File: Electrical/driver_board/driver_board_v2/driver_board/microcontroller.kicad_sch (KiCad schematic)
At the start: 28 parts, among them J1 USB_C_Receptacle_USB2.0_14P, U1 AMS1117-3.3, U1 STM32F446RETx, Y1 8Mhz

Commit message: Added full PSU architecture to driverboard
+24V In

+12V out
+5V out
+3.3V out
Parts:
- removed C13, C14: C, symbol Device:C
- removed D1: LED, symbol Device:LED
- removed R2: 1.5kΩ, symbol Device:R
- removed U1: AMS1117-3.3, Package_TO_SOT_SMD:SOT-223-3_TabPin2, symbol Regulator_Linear:AMS1117-3.3
- gave numbers to parts that had none: 3
- renumbered FB2 to FB1, R3 to R2, R1 to R3, R2 to R4

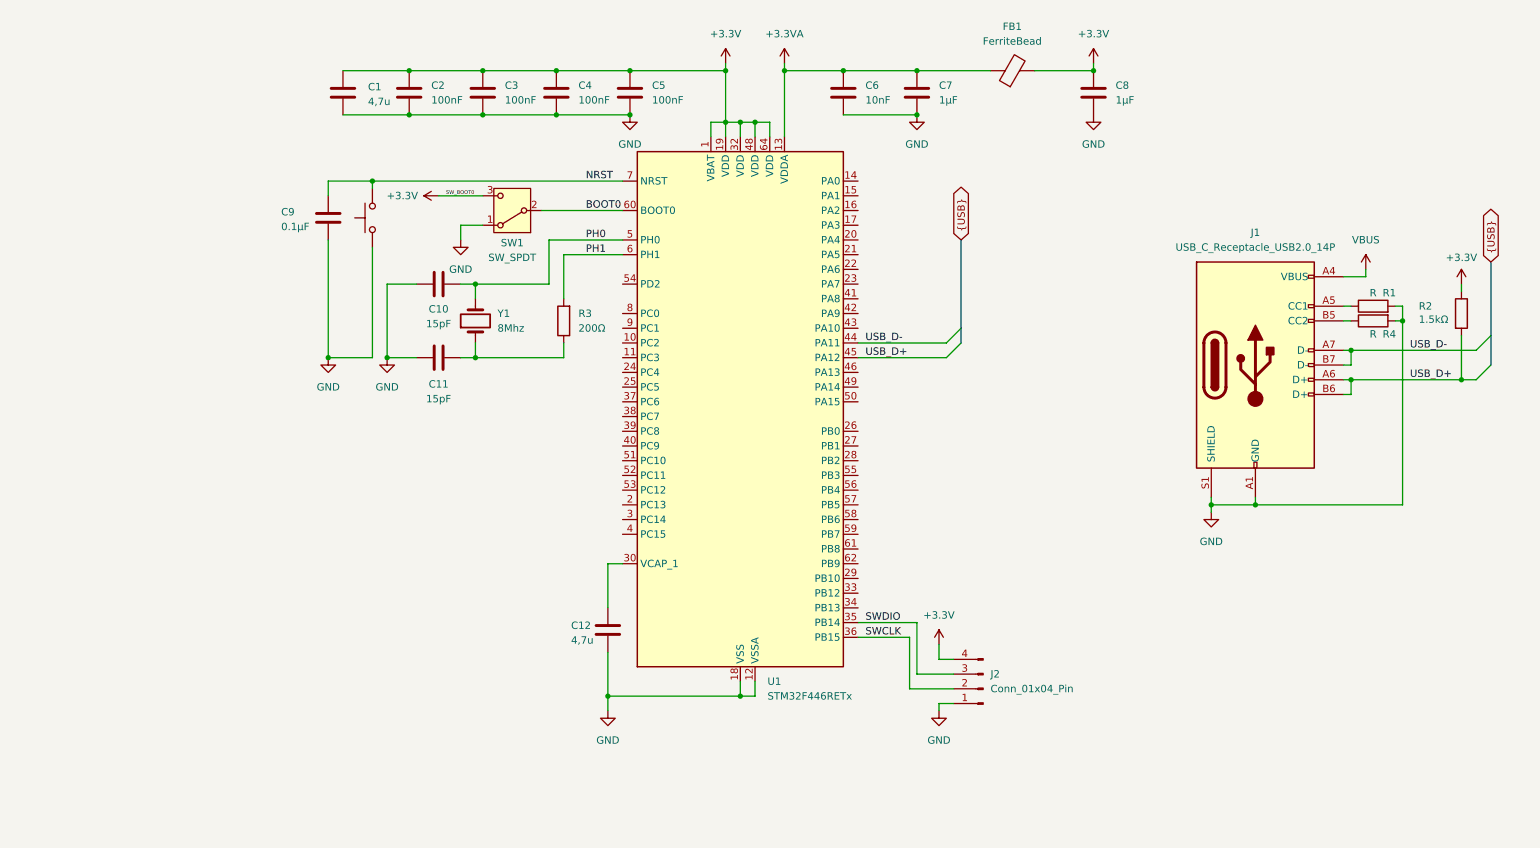
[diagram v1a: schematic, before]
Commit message: Cleaned up a bit and fixed mistake with NRST pin
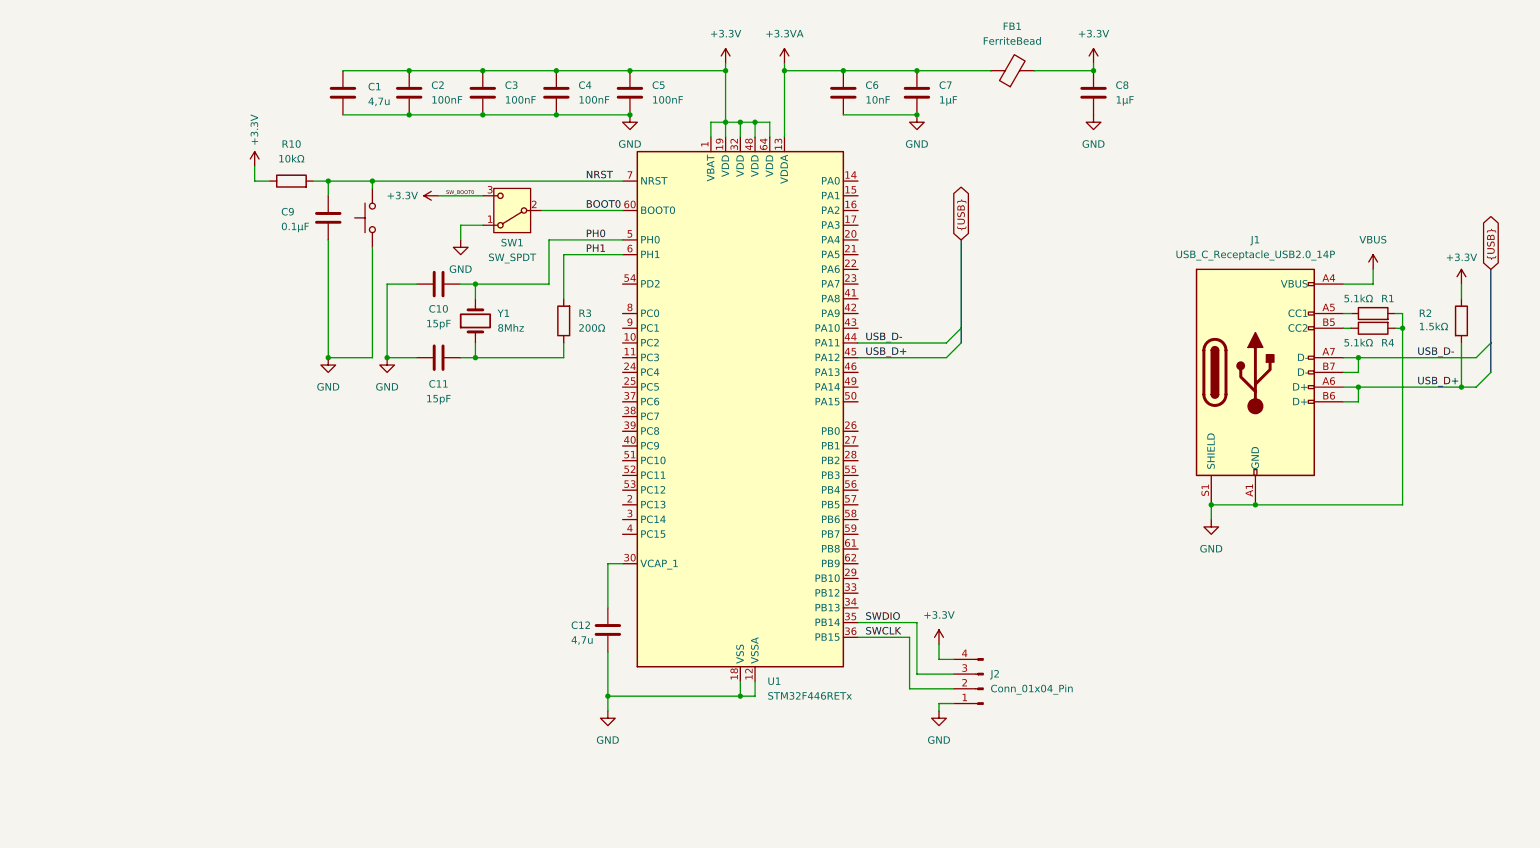
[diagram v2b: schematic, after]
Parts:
- added R10: 10kΩ, symbol Device:R
- R1, R4: value R -> 5.1kΩ
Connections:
- net +3.3V: now also R10.1
- net NRST: now also R10.2
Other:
- moved on the sheet: J1, R1, R2, R4

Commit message: Added footprint of motor driver and added power
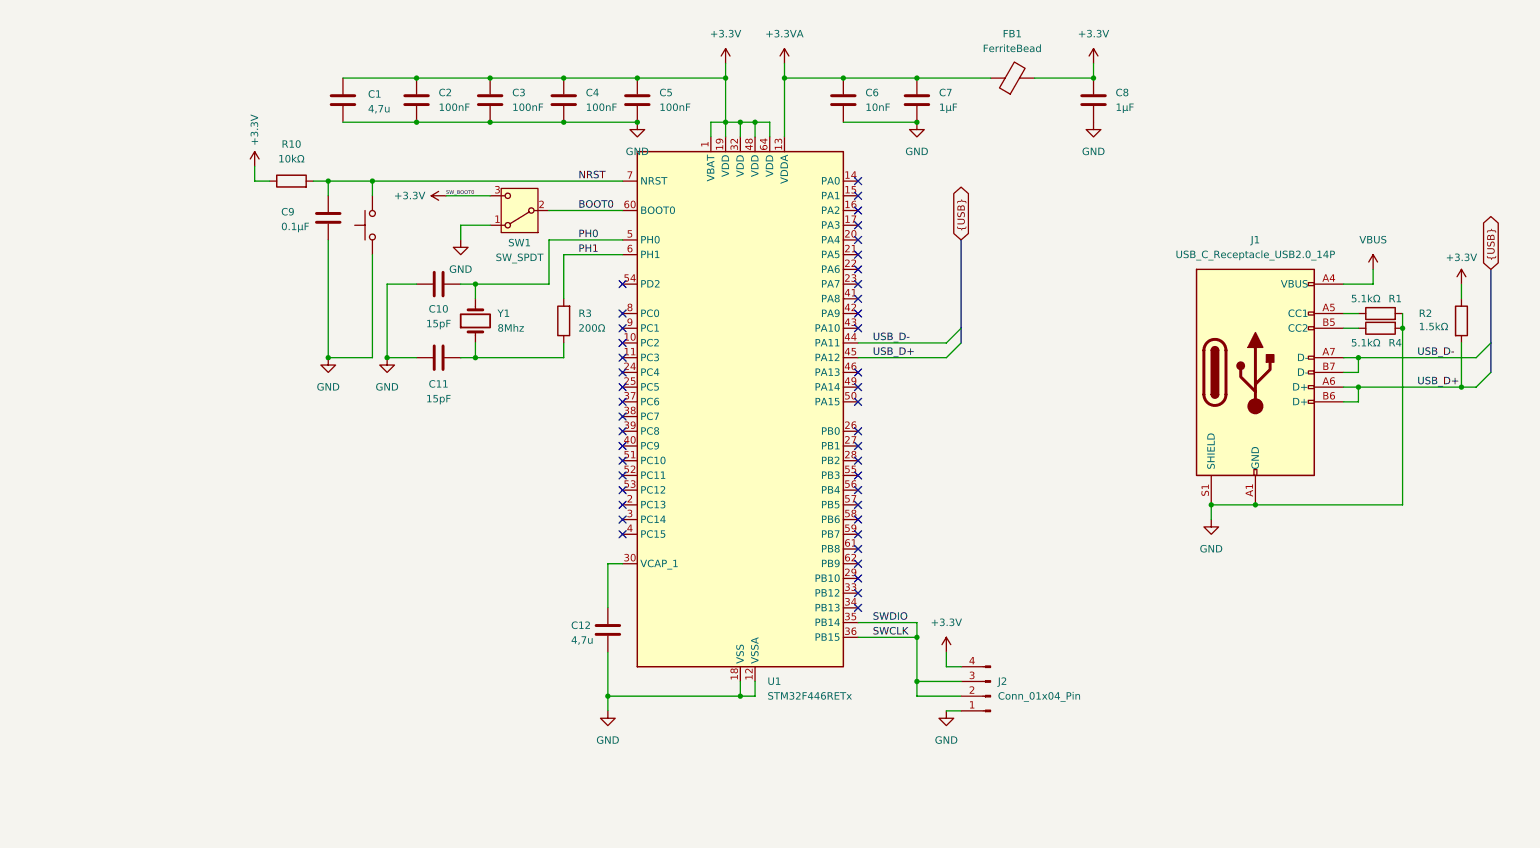
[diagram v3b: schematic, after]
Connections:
- net SWDIO is gone; now on net SWCLK: J2.3 (Pin_3), U1.35 (PB14)
- no-connect marks 0 -> 44
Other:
- moved on the sheet: C1, C2, C3, C4, C5, C6, C7, C8, FB1, J2, R1, R4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

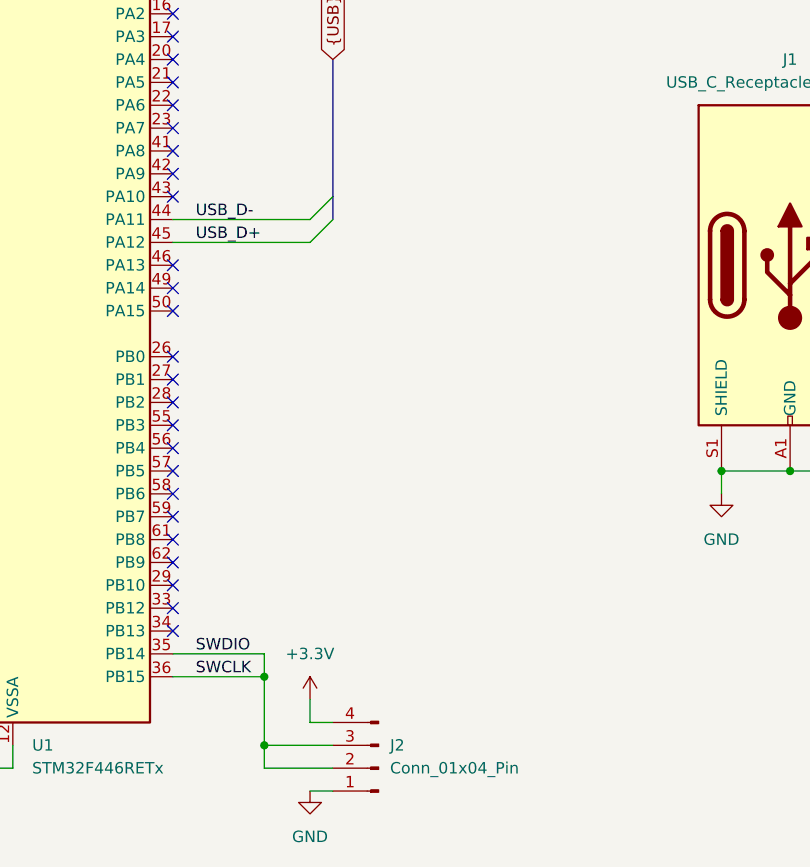
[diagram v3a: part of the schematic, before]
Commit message: Discovered critical error and changed pinout
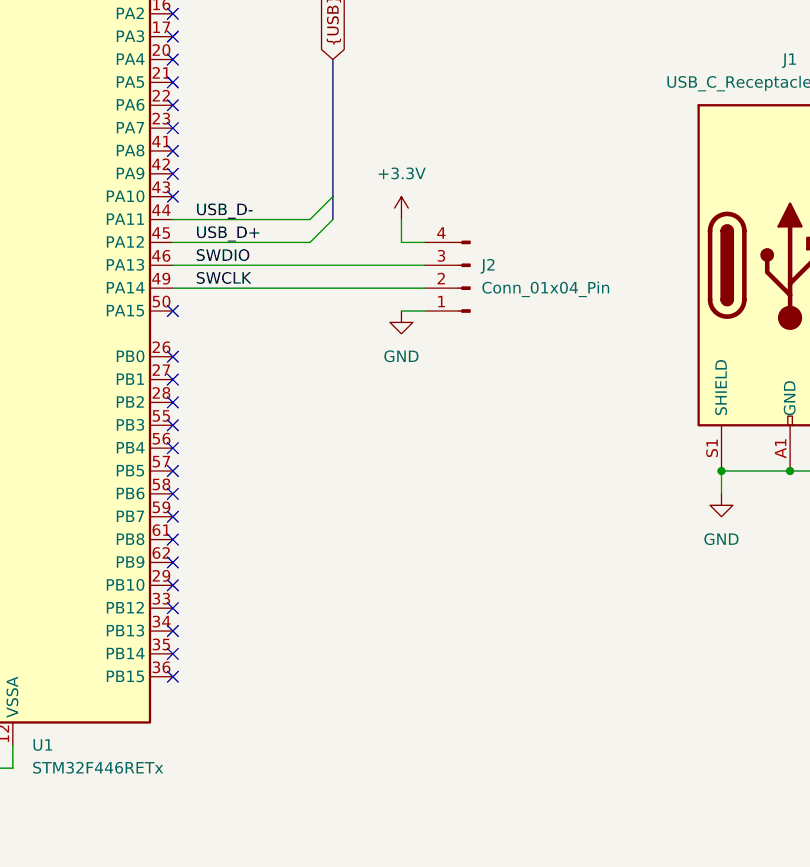
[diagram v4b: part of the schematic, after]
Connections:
- net SWCLK: now also U1.49 (PA14); no longer J2.3 (Pin_3), U1.35 (PB14), U1.36 (PB15)
- net SWDIO: now reaches U1.46 (PA13)
- net SWDIO: now also J2.3 (Pin_3)
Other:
- moved on the sheet: J2
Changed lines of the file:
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@@
 	(paper "A4")
 	(junction
-		(at 177.8 134.62)
-		(diameter 0)
-		(color 0 0 0 0)
-	)
-	(junction
 		(at 91.44 30.48)
 		(diameter 0)
@@
 	)
 	(junction
-		(at 177.8 127)
-		(diameter 0)
-		(color 0 0 0 0)
-	)
-	(junction
 		(at 228.6 104.14)
 		(diameter 0)
@@
 	)
 	(no_connect
-		(at 167.64 83.82)
+		(at 167.64 109.22)
 	)
 	(no_connect
-		(at 167.64 109.22)
+		(at 167.64 124.46)
 	)
 	(no_connect
@@
 	)
 	(no_connect
-		(at 127 81.28)
+		(at 167.64 127)
 	)
 	(no_connect
-		(at 167.64 55.88)
+		(at 127 81.28)
 	)
 	(no_connect
-		(at 167.64 81.28)
+		(at 167.64 55.88)
 	)
 	(no_connect
@@
 	(wire
 		(pts
-			(xy 177.8 134.62) (xy 177.8 127)
-		)
-		(stroke
-			(width 0)
-			(type default)
-		)
-	)
-	(wire
-		(pts
 			(xy 142.24 40.64) (xy 142.24 38.1)
 		)
@@
 	(wire
 		(pts
-			(xy 177.8 137.16) (xy 177.8 134.62)
-		)
-		(stroke
-			(width 0)
-			(type default)
-		)
-	)
-	(wire
-		(pts
 			(xy 99.06 55.88) (xy 104.14 55.88)
 		)
@@
 	(wire
 		(pts
-			(xy 177.8 137.16) (xy 185.42 137.16)
-		)
-		(stroke
-			(width 0)
-			(type default)
-		)
-	)
-	(wire
-		(pts
-			(xy 177.8 127) (xy 167.64 127)
-		)
-		(stroke
-			(width 0)
-			(type default)
-		)
-	)
-	(wire
-		(pts
 			(xy 76.2 48.26) (xy 76.2 50.8)
 		)
@@
 		)
 	)
-	(wire
+	(bus
 		(pts
-			(xy 182.88 132.08) (xy 182.88 129.54)
+			(xy 185.42 58.42) (xy 185.42 73.66)
 		)
 		(stroke
@@
 	(wire
 		(pts
-			(xy 177.8 127) (xy 177.8 124.46)
-		)
-		(stroke
-			(width 0)
-			(type default)
-		)
-	)
-	(bus
-		(pts
-			(xy 185.42 58.42) (xy 185.42 73.66)
+			(xy 271.78 83.82) (xy 274.32 83.82)
 		)
 		(stroke
@@
 	(wire
 		(pts
-			(xy 271.78 83.82) (xy 274.32 83.82)
+			(xy 152.4 38.1) (xy 152.4 40.64)
 		)
 		(stroke
@@
 	(wire
 		(pts
-			(xy 152.4 38.1) (xy 152.4 40.64)
+			(xy 124.46 114.3) (xy 127 114.3)
 		)
 		(stroke
@@
 	(wire
 		(pts
-			(xy 124.46 114.3) (xy 127 114.3)
+			(xy 86.36 66.04) (xy 86.36 78.74)
 		)
 		(stroke
@@
 	(wire
 		(pts
-			(xy 86.36 66.04) (xy 86.36 78.74)
+			(xy 193.04 76.2) (xy 193.04 78.74)
 		)
 		(stroke
@@
 	(wire
 		(pts
+			(xy 167.64 83.82) (xy 195.58 83.82)
+		)
+		(stroke
+			(width 0)
+			(type default)
+		)
+	)
+	(wire
+		(pts
 			(xy 91.44 38.1) (xy 104.14 38.1)
 		)
@@
 	(wire
 		(pts
-			(xy 185.42 132.08) (xy 182.88 132.08)
+			(xy 167.64 81.28) (xy 195.58 81.28)
 		)
 		(stroke
@@
 	(wire
 		(pts
-			(xy 185.42 139.7) (xy 182.88 139.7)
+			(xy 195.58 86.36) (xy 193.04 86.36)
 		)
 		(stroke
@@
 	(wire
 		(pts
+			(xy 193.04 78.74) (xy 195.58 78.74)
+		)
+		(stroke
+			(width 0)
+			(type default)
+		)
+	)
+	(wire
+		(pts
 			(xy 124.46 114.3) (xy 124.46 121.92)
 		)
@@
 	(wire
 		(pts
-			(xy 177.8 134.62) (xy 185.42 134.62)
-		)
-		(stroke
-			(width 0)
-			(type default)
-		)
-	)
-	(wire
-		(pts
 			(xy 91.44 66.04) (xy 86.36 66.04)
 		)
@@
 	(wire
 		(pts
-			(xy 177.8 124.46) (xy 167.64 124.46)
-		)
-		(stroke
-			(width 0)
-			(type default)
-		)
-	)
-	(wire
-		(pts
 			(xy 228.6 104.14) (xy 228.6 106.68)
 		)
@@
 	)
 	(label "SWDIO"
-		(at 170.18 124.46 0)
+		(at 170.18 81.28 0)
 		(effects
 			(font
@@
 	)
 	(label "SWCLK"
-		(at 170.18 127 0)
+		(at 170.18 83.82 0)
 		(effects
 			(font
@@
 	(symbol
 		(lib_id "power:GND")
-		(at 182.88 139.7 0)
+		(at 193.04 86.36 0)
 		(unit 1)
 		(exclude_from_sim no)
@@
 		(fields_autoplaced yes)
 		(property "Reference" "#PWR016"
-			(at 182.88 146.05 0)
+			(at 193.04 92.71 0)
 			(effects
 				(font
@@
 		)
 		(property "Value" "GND"
-			(at 182.88 144.78 0)
+			(at 193.04 91.44 0)
 			(effects
 				(font
@@
 		)
 		(property "Footprint" ""
-			(at 182.88 139.7 0)
+			(at 193.04 86.36 0)
 			(effects
 				(font
@@
 		)
 		(property "Datasheet" ""
-			(at 182.88 139.7 0)
+			(at 193.04 86.36 0)
 			(effects
 				(font
@@
 		)
 		(property "Description" "Power symbol creates a global label with name \"GND\" , ground"
-			(at 182.88 139.7 0)
+			(at 193.04 86.36 0)
 			(effects
 				(font
@@
 	(symbol
 		(lib_id "Connector:Conn_01x04_Pin")
-		(at 190.5 137.16 180)
+		(at 200.66 83.82 180)
 		(unit 1)
 		(exclude_from_sim no)
@@
 		(fields_autoplaced yes)
 		(property "Reference" "J2"
-			(at 191.77 134.6199 0)
+			(at 201.93 81.2799 0)
 			(effects
 				(font
@@
 		)
 		(property "Value" "Conn_01x04_Pin"
-			(at 191.77 137.1599 0)
+			(at 201.93 83.8199 0)
 			(effects
 				(font
@@
 		)
 		(property "Footprint" ""
-			(at 190.5 137.16 0)
+			(at 200.66 83.82 0)
 			(effects
 				(font
@@
 		)
 		(property "Datasheet" "~"
-			(at 190.5 137.16 0)
+			(at 200.66 83.82 0)
 			(effects
 				(font
@@
 		)
 		(property "Description" "Generic connector, single row, 01x04, script generated"
-			(at 190.5 137.16 0)
+			(at 200.66 83.82 0)
 			(effects
 				(font
@@
 	(symbol
 		(lib_id "power:+3.3V")
-		(at 182.88 129.54 0)
+		(at 193.04 76.2 0)
 		(unit 1)
 		(exclude_from_sim no)
@@
 		(fields_autoplaced yes)
 		(property "Reference" "#PWR014"
-			(at 182.88 133.35 0)
+			(at 193.04 80.01 0)
 			(effects
 				(font
@@
 		)
 		(property "Value" "+3.3V"
-			(at 182.88 124.46 0)
+			(at 193.04 71.12 0)
 			(effects
 				(font
@@
 		)
 		(property "Footprint" ""
-			(at 182.88 129.54 0)
+			(at 193.04 76.2 0)
 			(effects
 				(font
@@
 		)
 		(property "Datasheet" ""
-			(at 182.88 129.54 0)
+			(at 193.04 76.2 0)
 			(effects
 				(font
@@
 		)
 		(property "Description" "Power symbol creates a global label with name \"+3.3V\""
-			(at 182.88 129.54 0)
+			(at 193.04 76.2 0)
 			(effects
 				(font
